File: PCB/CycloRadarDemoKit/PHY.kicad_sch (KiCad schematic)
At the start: 34 parts, among them J201 ARJM11B1-009-AB-EW2, U201 IP101GRI, Y201 25MHz

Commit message: layout mockup done
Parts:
- J201: footprint Connector_RJ:RJ45_OST_PJ012-8P8CX_Vertical -> Connector_RJ:CONN12_5-2301995-3_TEC
- TP201, TP202, TP203: footprint TestPoint:TestPoint_Pad_D2.0mm -> TestPoint:TestPoint_Pad_D1.0mm
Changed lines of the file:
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@@
       (effects (font (size 1.27 1.27)) (justify left))
     )
-    (property "Footprint" "TestPoint:TestPoint_Pad_D2.0mm" (at 215.9 45.72 0)
+    (property "Footprint" "TestPoint:TestPoint_Pad_D1.0mm" (at 215.9 45.72 0)
       (effects (font (size 1.27 1.27)) hide)
     )
@@
       (effects (font (size 1.27 1.27)) (justify left))
     )
-    (property "Footprint" "TestPoint:TestPoint_Pad_D2.0mm" (at 86.36 48.26 0)
+    (property "Footprint" "TestPoint:TestPoint_Pad_D1.0mm" (at 86.36 48.26 0)
       (effects (font (size 1.27 1.27)) hide)
     )
@@
       (effects (font (size 1.27 1.27)))
     )
-    (property "Footprint" "Connector_RJ:RJ45_OST_PJ012-8P8CX_Vertical" (at 71.12 130.81 0)
+    (property "Footprint" "Connector_RJ:CONN12_5-2301995-3_TEC" (at 71.12 130.81 0)
       (effects (font (size 1.27 1.27)) hide)
     )
@@
       (effects (font (size 1.27 1.27)) (justify left))
     )
-    (property "Footprint" "TestPoint:TestPoint_Pad_D2.0mm" (at 190.5 82.55 0)
-      (effects (font (size 1.27 1.27)) hide)
-    )
+    (property "Footprint" "TestPoint:TestPoint_Pad_D1.0mm" (at 190.5 82.55 0)
+      (effects (font (size 1.27 1.27)) hide)
+    )

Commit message: PCB, 3Dmodel
mockup PCB version done, schcematic exported to latex, 3D model generated and exported to latex
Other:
- title: Safety Ride Radar Sensor -> Radar Safety Sensor
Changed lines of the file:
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@@
   (paper "A4")
   (title_block
-    (title "Safety Ride Radar Sensor")
-    (date "2023-12-19")
-    (rev "Rev.: WIP")
+    (title "Radar Safety Sensor")
+    (date "2023-12-20")
+    (rev "Rev.: 1")
     (company "ALPS Electric Czech, s.r.o.")
     (comment 1 "Designed by Martin Tavoda")

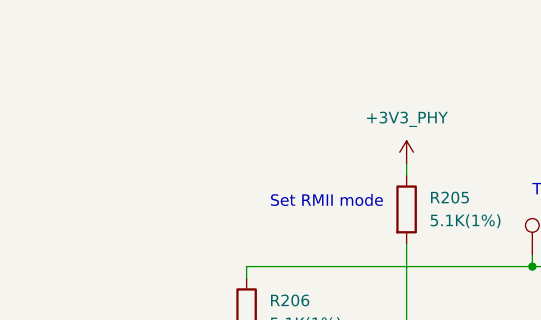
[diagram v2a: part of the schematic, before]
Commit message: sortingAbbr, cosmetics schematic, export schematic to thesis
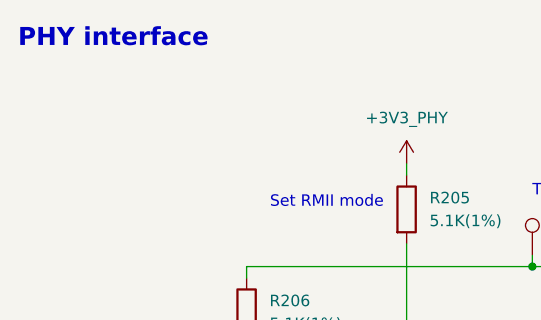
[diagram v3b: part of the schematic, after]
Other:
- note added: "PHY interface"
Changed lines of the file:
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@@
     (title "Radar Safety Sensor")
     (date "2023-12-20")
-    (rev "Rev.: 1")
+    (rev "Rev.: 1.0")
     (company "ALPS Electric Czech, s.r.o.")
     (comment 1 "Designed by Martin Tavoda")
@@
     (effects (font (size 2 2) (thickness 0.4) bold) (justify left bottom))
   )
+  (text "PHY interface" (at 24.13 25.4 0)
+    (effects (font (size 2 2) (thickness 0.4) bold) (justify left bottom))
+  )

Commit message: PCB small updates, schemtatic cosmetics, SEP FINAL
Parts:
- removed J201: ARJM11B1-009-AB-EW2, Connector_RJ:CONN12_5-2301995-3_TEC, symbol Connector:RJ45_100Base-T
- added J302: TMJD0012BENL, Connector_RJ:RJ45_Taoglas_TMJD0012BENL, symbol Connector:RJ45_Taoglas_TMJD0012BENL
- C208, C209: footprint (none) -> Capacitor_SMD:C_0402_1005Metric; LCSC (none) -> C182483
- Y201: LCSC C124313 -> C3003239
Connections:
- net +3V3_PHY: now also J302.11
- net GND: now also C212.1; no longer C212.2
- net LED3/PHY_AD3: now also J302.9
- net RD+: now also J302.4 (RD+)
- net RD-: now also J302.6 (RD-)
- net TD+: now also J302.1 (TD+)
- net TD-: now also J302.3 (TD-)
- net at C210.1, C211.1: now also J302.2 (TCT), J302.5 (RCT)
- net GNDPWR: now reaches C213.1
- net GNDPWR: now also C212.2, J302.14, J302.16, J302.8; no longer C212.1
- net at R211.2: now also J302.10
- net at R213.2: now also J302.12
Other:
- moved on the sheet: C212, C213

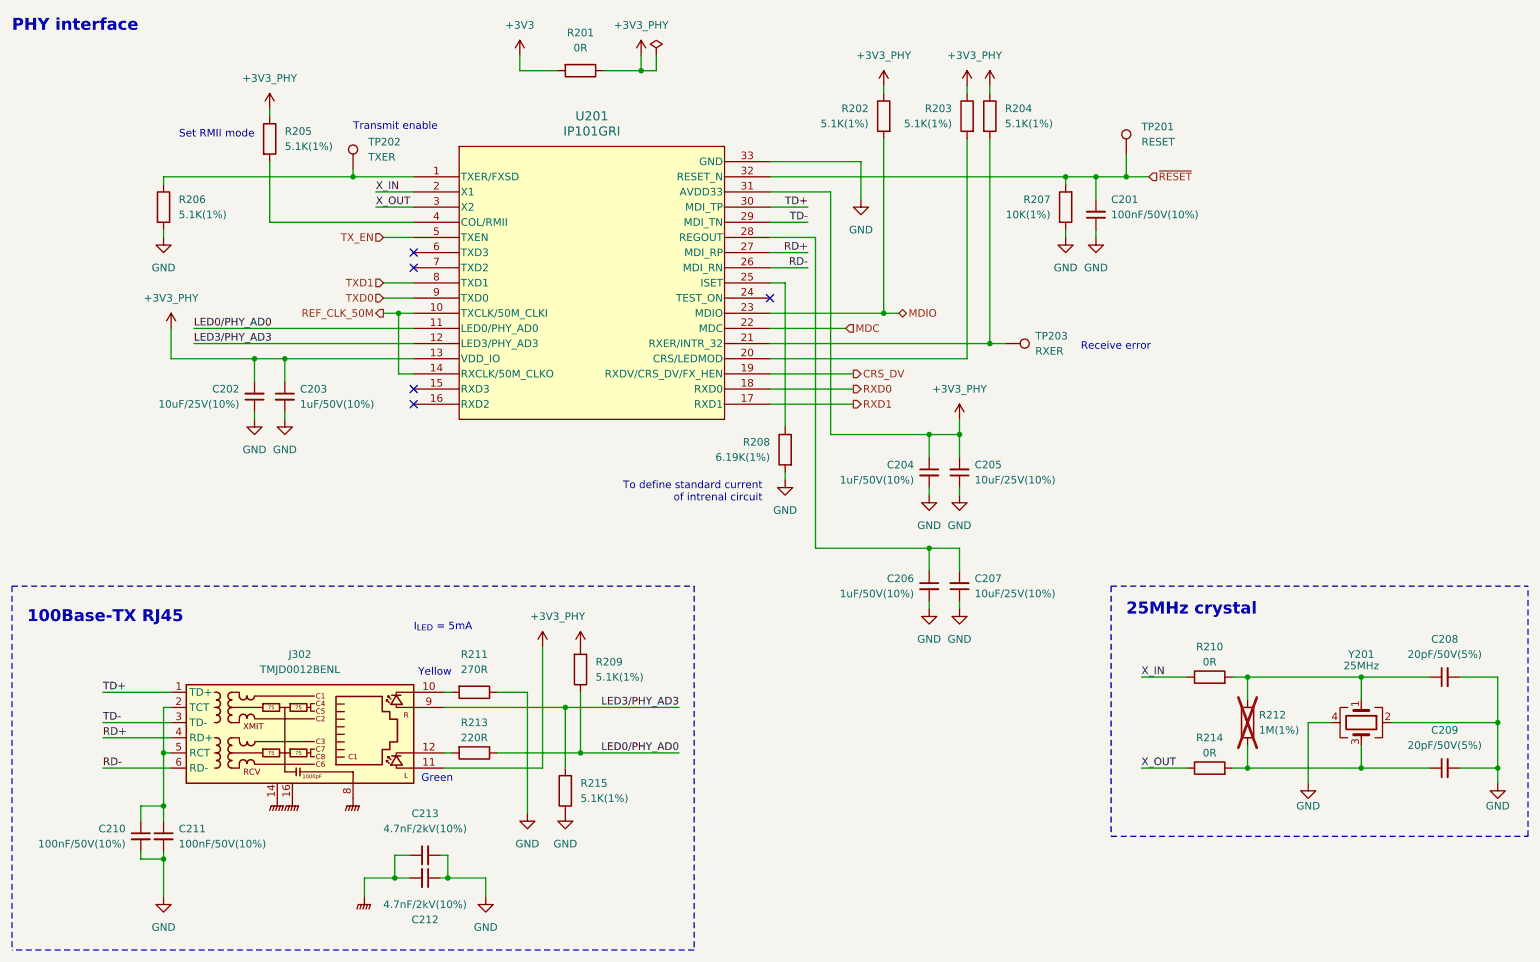
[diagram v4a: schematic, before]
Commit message: reanotated schematic, routing started
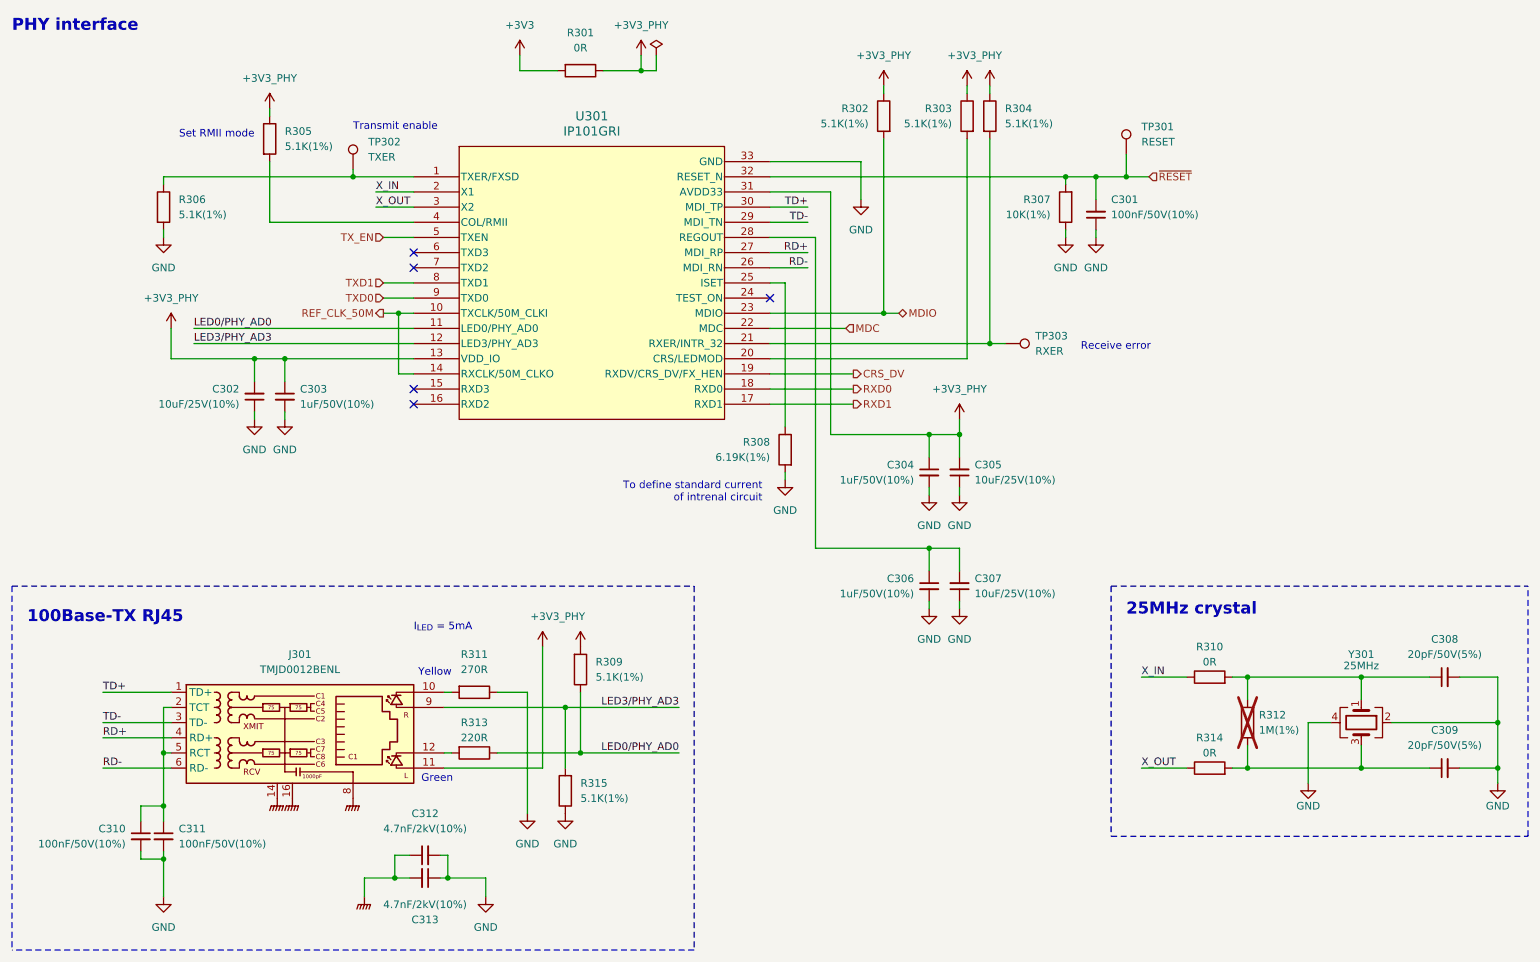
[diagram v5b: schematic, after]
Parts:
- R310: renamed from R210; footprint Resistor_SMD:R_0805_2012Metric -> Resistor_SMD:R_0603_1608Metric; LCSC C17477 -> C21189
- R312: renamed from R212; LCSC C22935 -> (none)
- R314: renamed from R214; footprint Resistor_SMD:R_0805_2012Metric -> Resistor_SMD:R_0603_1608Metric; LCSC C17477 -> C21189
- renumbered C201 to C301, C202 to C302, C203 to C303, C204 to C304, C205 to C305, C206 to C306, C207 to C307, C208 to C308, C209 to C309, C210 to C310, C211 to C311, C213 to C312, C212 to C313, J302 to J301, R201 to R301, R202 to R302, R203 to R303, R204 to R304, R205 to R305, R206 to R306, R207 to R307, R208 to R308, R209 to R309, R211 to R311, R213 to R313, R215 to R315, TP201 to TP301, TP202 to TP302, TP203 to TP303, U201 to U301, Y201 to Y301

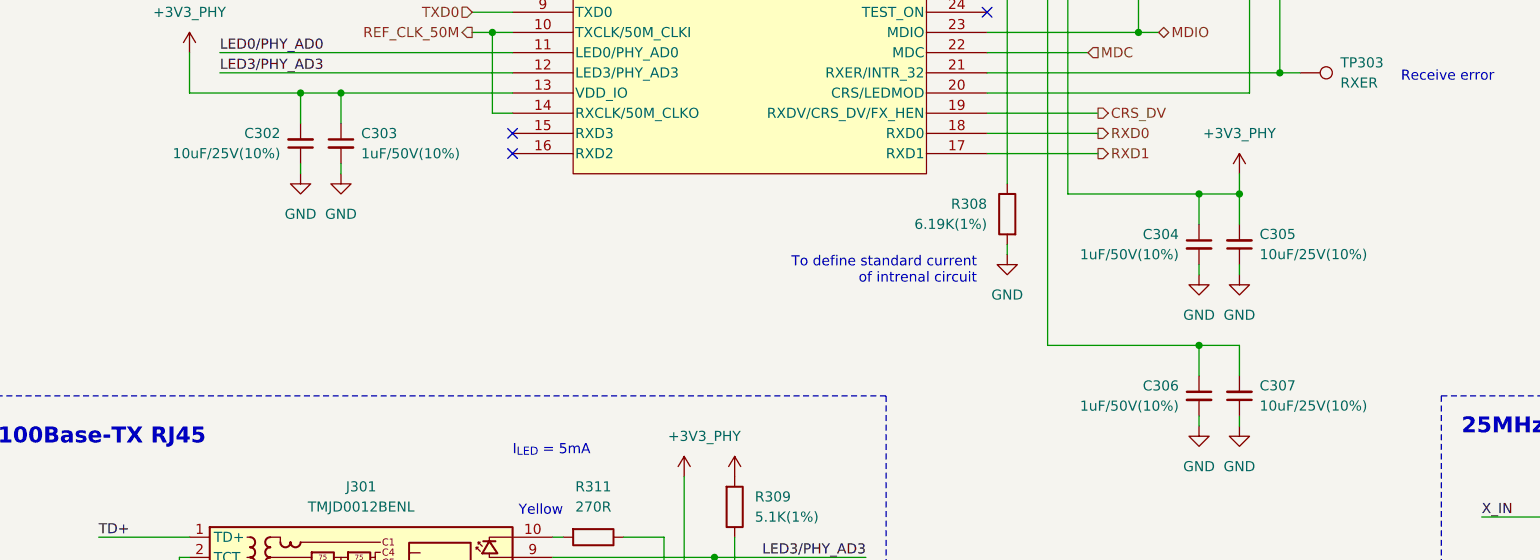
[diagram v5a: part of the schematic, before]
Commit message: Parts ordered on PCB, 1206->0803 10uF, 0803->0402 1uF
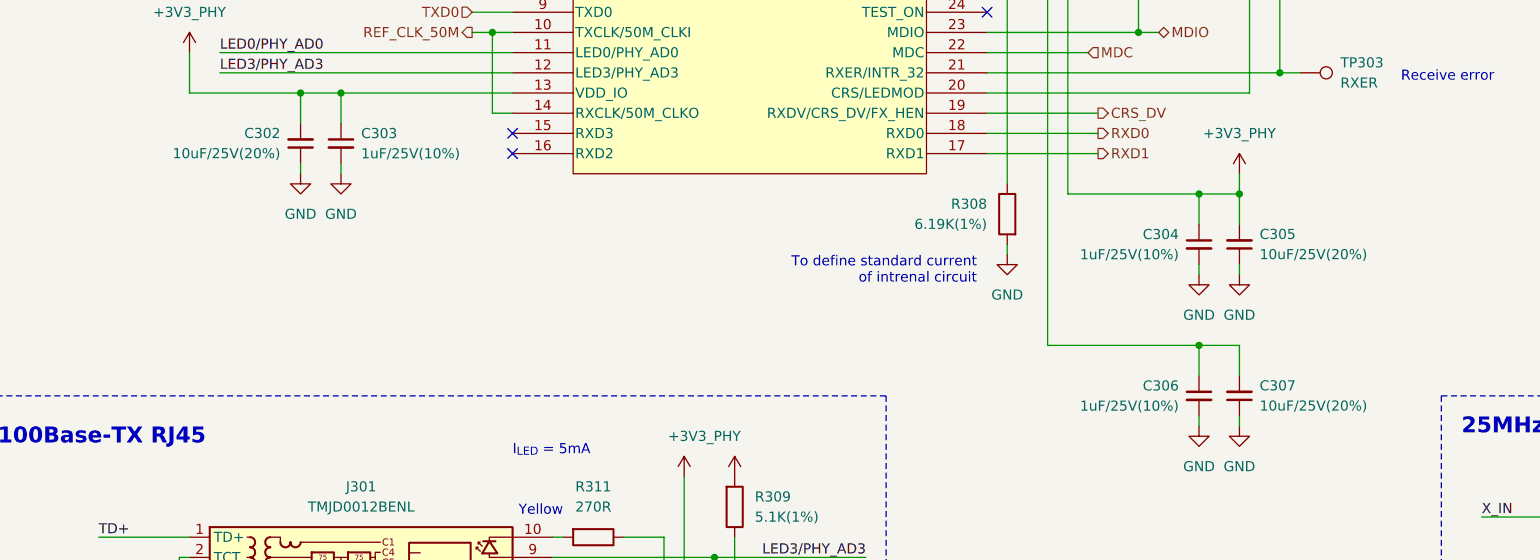
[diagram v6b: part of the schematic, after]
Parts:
- C302, C305, C307: value 10uF/25V(10%) -> 10uF/25V(20%); footprint Capacitor_SMD:C_1206_3216Metric -> Capacitor_SMD:C_0603_1608Metric; LCSC C77090 -> C96446
- C303, C304, C306: value 1uF/50V(10%) -> 1uF/25V(10%); footprint Capacitor_SMD:C_0603_1608Metric -> Capacitor_SMD:C_0402_1005Metric; LCSC C15849 -> C52923
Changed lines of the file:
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@@
       (effects (font (size 1.27 1.27)) (justify right))
     )
-    (property "Value" "10uF/25V(10%)" (at 62.23 87.6236 0)
+    (property "Value" "10uF/25V(20%)" (at 62.23 87.6236 0)
       (effects (font (size 1.27 1.27)) (justify right))
     )
-    (property "Footprint" "Capacitor_SMD:C_1206_3216Metric" (at 64.77 86.36 0)
+    (property "Footprint" "Capacitor_SMD:C_0603_1608Metric" (at 64.77 86.36 0)
       (effects (font (size 1.27 1.27)) hide)
     )
@@
       (effects (font (size 1.27 1.27)) hide)
     )
-    (property "LCSC" "C77090" (at 64.77 86.36 0)
+    (property "LCSC" "C96446" (at 64.77 86.36 0)
       (effects (font (size 1.27 1.27)) hide)
     )
@@
       (effects (font (size 1.27 1.27)) (justify left))
     )
-    (property "Value" "1uF/50V(10%)" (at 175.26 119.3863 0)
-      (effects (font (size 1.27 1.27)) (justify left))
-    )
-    (property "Footprint" "Capacitor_SMD:C_0603_1608Metric" (at 177.8 118.11 0)
+    (property "Value" "1uF/25V(10%)" (at 175.26 119.3863 0)
+      (effects (font (size 1.27 1.27)) (justify left))
+    )
+    (property "Footprint" "Capacitor_SMD:C_0402_1005Metric" (at 177.8 118.11 0)
       (effects (font (size 1.27 1.27)) hide)
     )
@@
       (effects (font (size 1.27 1.27)) hide)
     )
-    (property "LCSC" "C15849" (at 177.8 118.11 0)
+    (property "LCSC" "C52923" (at 177.8 118.11 0)
       (effects (font (size 1.27 1.27)) hide)
     )
@@
       (effects (font (size 1.27 1.27)) (justify left))
     )
-    (property "Value" "1uF/50V(10%)" (at 72.39 87.6363 0)
-      (effects (font (size 1.27 1.27)) (justify left))
-    )
-    (property "Footprint" "Capacitor_SMD:C_0603_1608Metric" (at 69.85 86.36 0)
+    (property "Value" "1uF/25V(10%)" (at 72.39 87.6363 0)
+      (effects (font (size 1.27 1.27)) (justify left))
+    )
+    (property "Footprint" "Capacitor_SMD:C_0402_1005Metric" (at 69.85 86.36 0)
       (effects (font (size 1.27 1.27)) hide)
     )
@@
       (effects (font (size 1.27 1.27)) hide)
     )
-    (property "LCSC" "C15849" (at 69.85 86.36 0)
+    (property "LCSC" "C52923" (at 69.85 86.36 0)
       (effects (font (size 1.27 1.27)) hide)
     )
@@
       (effects (font (size 1.27 1.27)) (justify right))
     )
-    (property "Value" "10uF/25V(10%)" (at 185.42 100.3236 0)
+    (property "Value" "10uF/25V(20%)" (at 185.42 100.3236 0)
       (effects (font (size 1.27 1.27)) (justify right))
     )
-    (property "Footprint" "Capacitor_SMD:C_1206_3216Metric" (at 182.88 99.06 0)
+    (property "Footprint" "Capacitor_SMD:C_0603_1608Metric" (at 182.88 99.06 0)
       (effects (font (size 1.27 1.27)) hide)
     )
@@
       (effects (font (size 1.27 1.27)) hide)
     )
-    (property "LCSC" "C77090" (at 182.88 99.06 0)
+    (property "LCSC" "C96446" (at 182.88 99.06 0)
       (effects (font (size 1.27 1.27)) hide)
     )
@@
       (effects (font (size 1.27 1.27)) (justify left))
     )
-    (property "Value" "1uF/50V(10%)" (at 175.26 100.3363 0)
-      (effects (font (size 1.27 1.27)) (justify left))
-    )
-    (property "Footprint" "Capacitor_SMD:C_0603_1608Metric" (at 177.8 99.06 0)
+    (property "Value" "1uF/25V(10%)" (at 175.26 100.3363 0)
+      (effects (font (size 1.27 1.27)) (justify left))
+    )
+    (property "Footprint" "Capacitor_SMD:C_0402_1005Metric" (at 177.8 99.06 0)
       (effects (font (size 1.27 1.27)) hide)
     )
@@
       (effects (font (size 1.27 1.27)) hide)
     )
-    (property "LCSC" "C15849" (at 177.8 99.06 0)
+    (property "LCSC" "C52923" (at 177.8 99.06 0)
       (effects (font (size 1.27 1.27)) hide)
     )
@@
       (effects (font (size 1.27 1.27)) (justify right))
     )
-    (property "Value" "10uF/25V(10%)" (at 185.42 119.3736 0)
+    (property "Value" "10uF/25V(20%)" (at 185.42 119.3736 0)
       (effects (font (size 1.27 1.27)) (justify right))
     )
-    (property "Footprint" "Capacitor_SMD:C_1206_3216Metric" (at 182.88 118.11 0)
+    (property "Footprint" "Capacitor_SMD:C_0603_1608Metric" (at 182.88 118.11 0)
       (effects (font (size 1.27 1.27)) hide)
     )
@@
       (effects (font (size 1.27 1.27)) hide)
     )
-    (property "LCSC" "C77090" (at 182.88 118.11 0)
-      (effects (font (size 1.27 1.27)) hide)
-    )
+    (property "LCSC" "C96446" (at 182.88 118.11 0)
+      (effects (font (size 1.27 1.27)) hide)
+    )

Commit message: USB layout, long traces from upper prepaired
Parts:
- TP301, TP302, TP303: now left out of the parts list
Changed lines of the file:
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@@
   )
   (symbol (lib_id "Connector:TestPoint") (at 210.82 45.72 0) (unit 1)
-    (in_bom yes) (on_board yes) (dnp no) (fields_autoplaced)
+    (in_bom no) (on_board yes) (dnp no) (fields_autoplaced)
     (property "Reference" "TP301" (at 213.36 41.148 0)
       (effects (font (size 1.27 1.27)) (justify left))
@@
   )
   (symbol (lib_id "Connector:TestPoint") (at 81.28 48.26 0) (unit 1)
-    (in_bom yes) (on_board yes) (dnp no) (fields_autoplaced)
+    (in_bom no) (on_board yes) (dnp no) (fields_autoplaced)
     (property "Reference" "TP302" (at 83.82 43.688 0)
       (effects (font (size 1.27 1.27)) (justify left))
@@
   )
   (symbol (lib_id "Connector:TestPoint") (at 190.5 77.47 270) (unit 1)
-    (in_bom yes) (on_board yes) (dnp no) (fields_autoplaced)
+    (in_bom no) (on_board yes) (dnp no) (fields_autoplaced)
     (property "Reference" "TP303" (at 195.58 76.2 90)
       (effects (font (size 1.27 1.27)) (justify left))
